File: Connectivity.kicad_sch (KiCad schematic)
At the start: 3 parts, among them U1 ESP32-C3-DevKitM-1

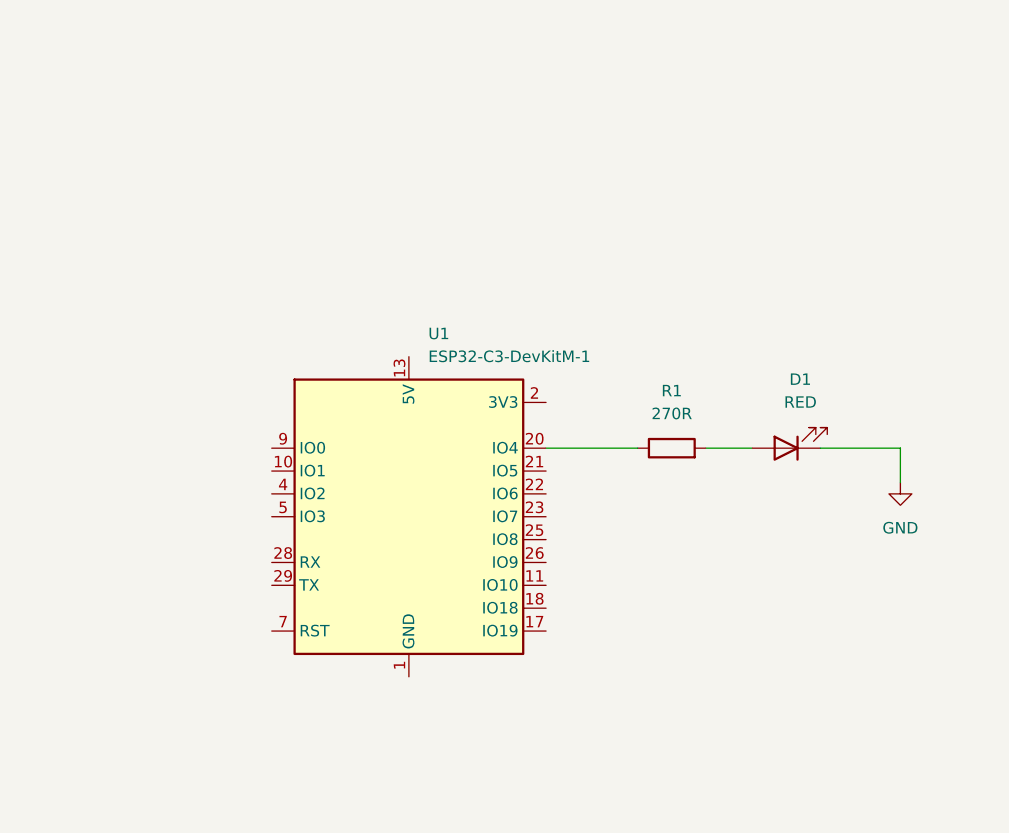
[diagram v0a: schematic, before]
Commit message: Lesson 2 - transistor circuits added
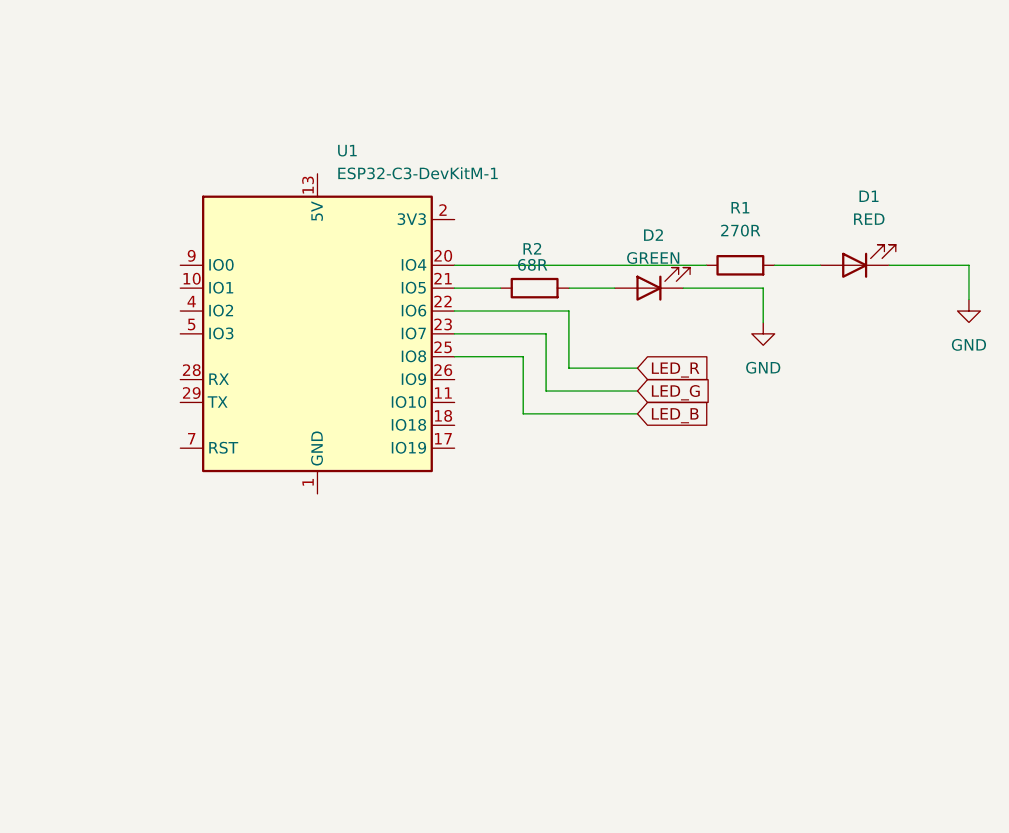
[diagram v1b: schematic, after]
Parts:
- added D2: GREEN, LED_SMD:LED_1206_3216Metric_Pad1.42x1.75mm_HandSolder, symbol Device:LED
- added R2: 68R, Resistor_SMD:R_1206_3216Metric, symbol Device:R
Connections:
- net GND: now also D2.1 (K)
- net at U1.21 (IO5): now also R2.1
- net LED_R: now reaches U1.22 (IO6)
- net LED_G: now reaches U1.23 (IO7)
- net LED_B: now reaches U1.25 (IO8)
- new net: D2.2 (A), R2.2
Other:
- moved on the sheet: D1, R1, U1

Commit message: Lesson 4 - Power Supply
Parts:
- added C4, C5: 100n/25V, Capacitor_SMD:C_1206_3216Metric, symbol Device:C
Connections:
- net GND: now also U1.1 (GND), U1.12 (GND), U1.15 (GND), U1.16 (GND), U1.19 (GND), U1.24 (GND), U1.27 (GND), U1.30 (GND), U1.6 (GND), U1.8 (GND), C4.2, C5.2
- net LED_B: now also U1.23 (IO7); no longer U1.25 (IO8)
- net LED_G: now also U1.22 (IO6); no longer U1.23 (IO7)
- net LED_R: now also U1.21 (IO5); no longer U1.22 (IO6)
- net at R2.1: no longer U1.21 (IO5)
- net +5V: now reaches U1.13 (5V), U1.14 (5V)
- net +5V: now also C4.1
- net +3V3: now reaches U1.2 (3V3), U1.3 (3V3)
- net +3V3: now also C5.1
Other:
- moved on the sheet: D2, R2
